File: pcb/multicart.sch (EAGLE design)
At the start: 17 parts, among them IC1 27C64-27C080, IC2 74HCT373N, IC3 74HCT08N, Q1 BS170

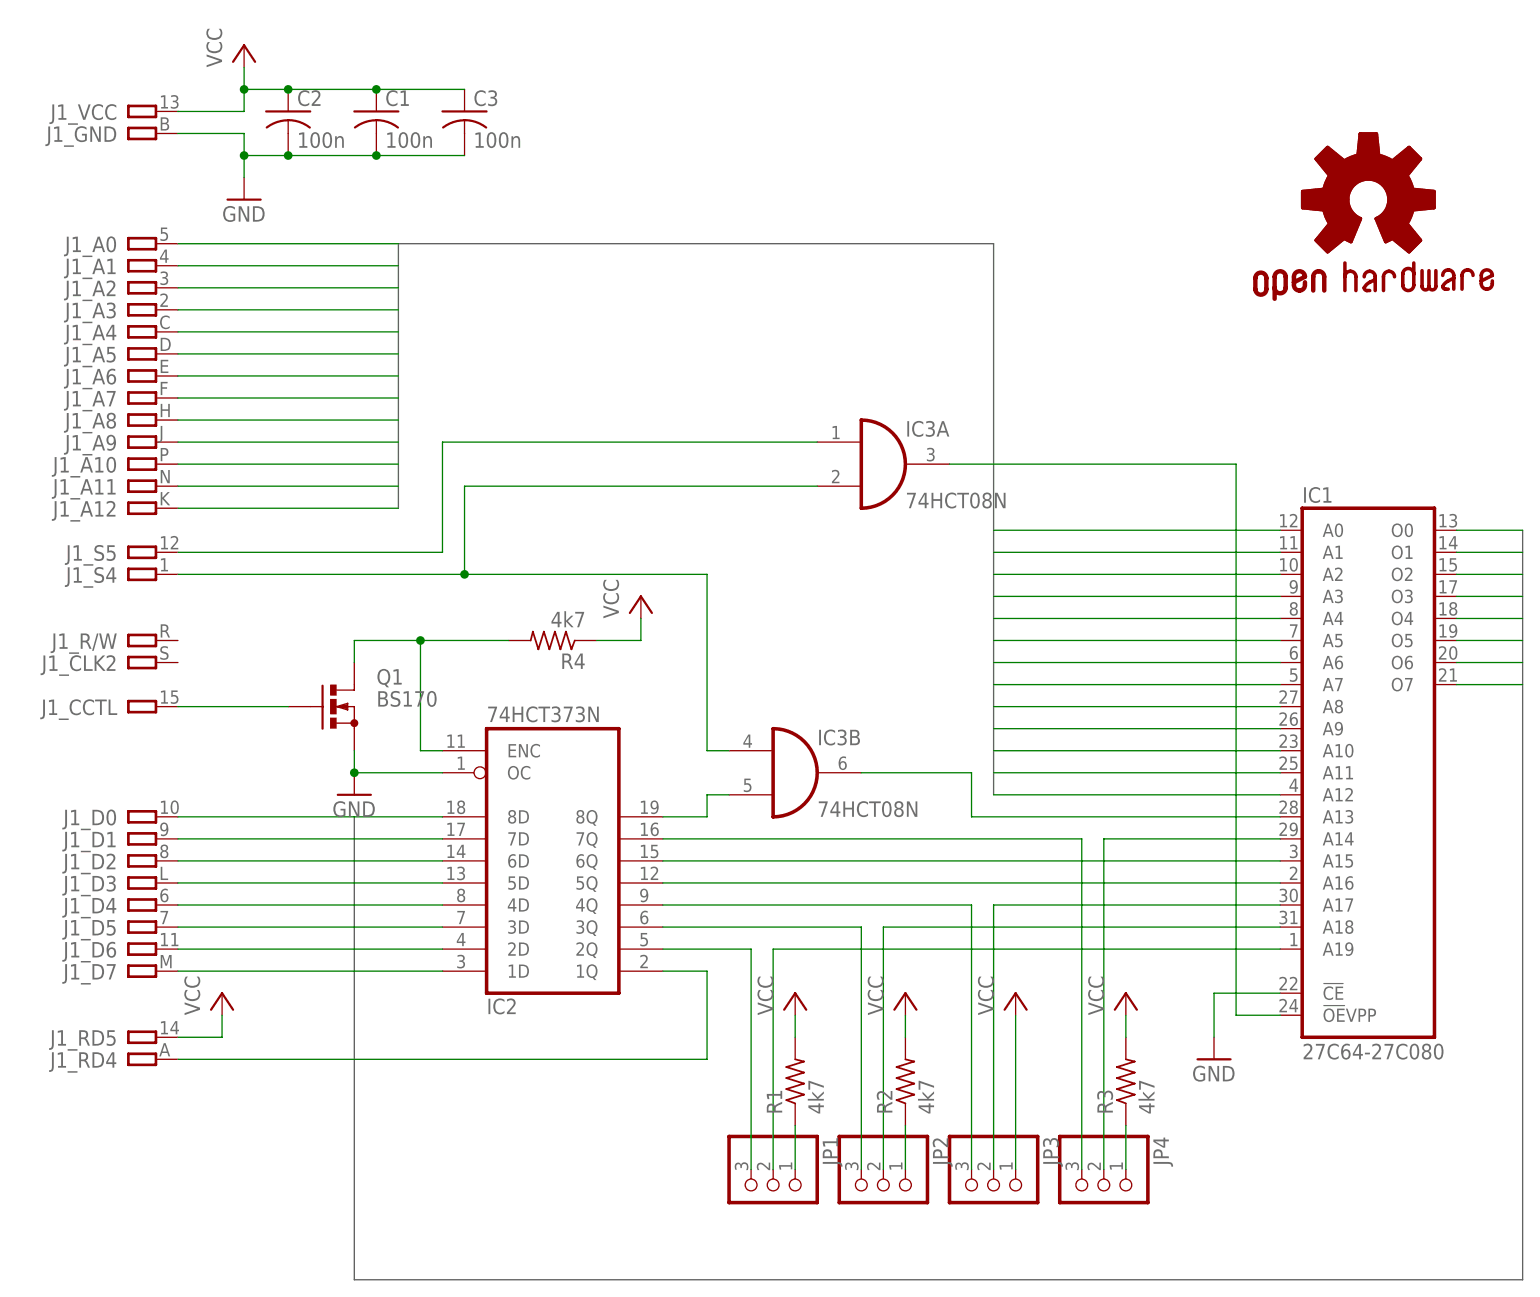
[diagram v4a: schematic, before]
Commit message: Added test points for power.
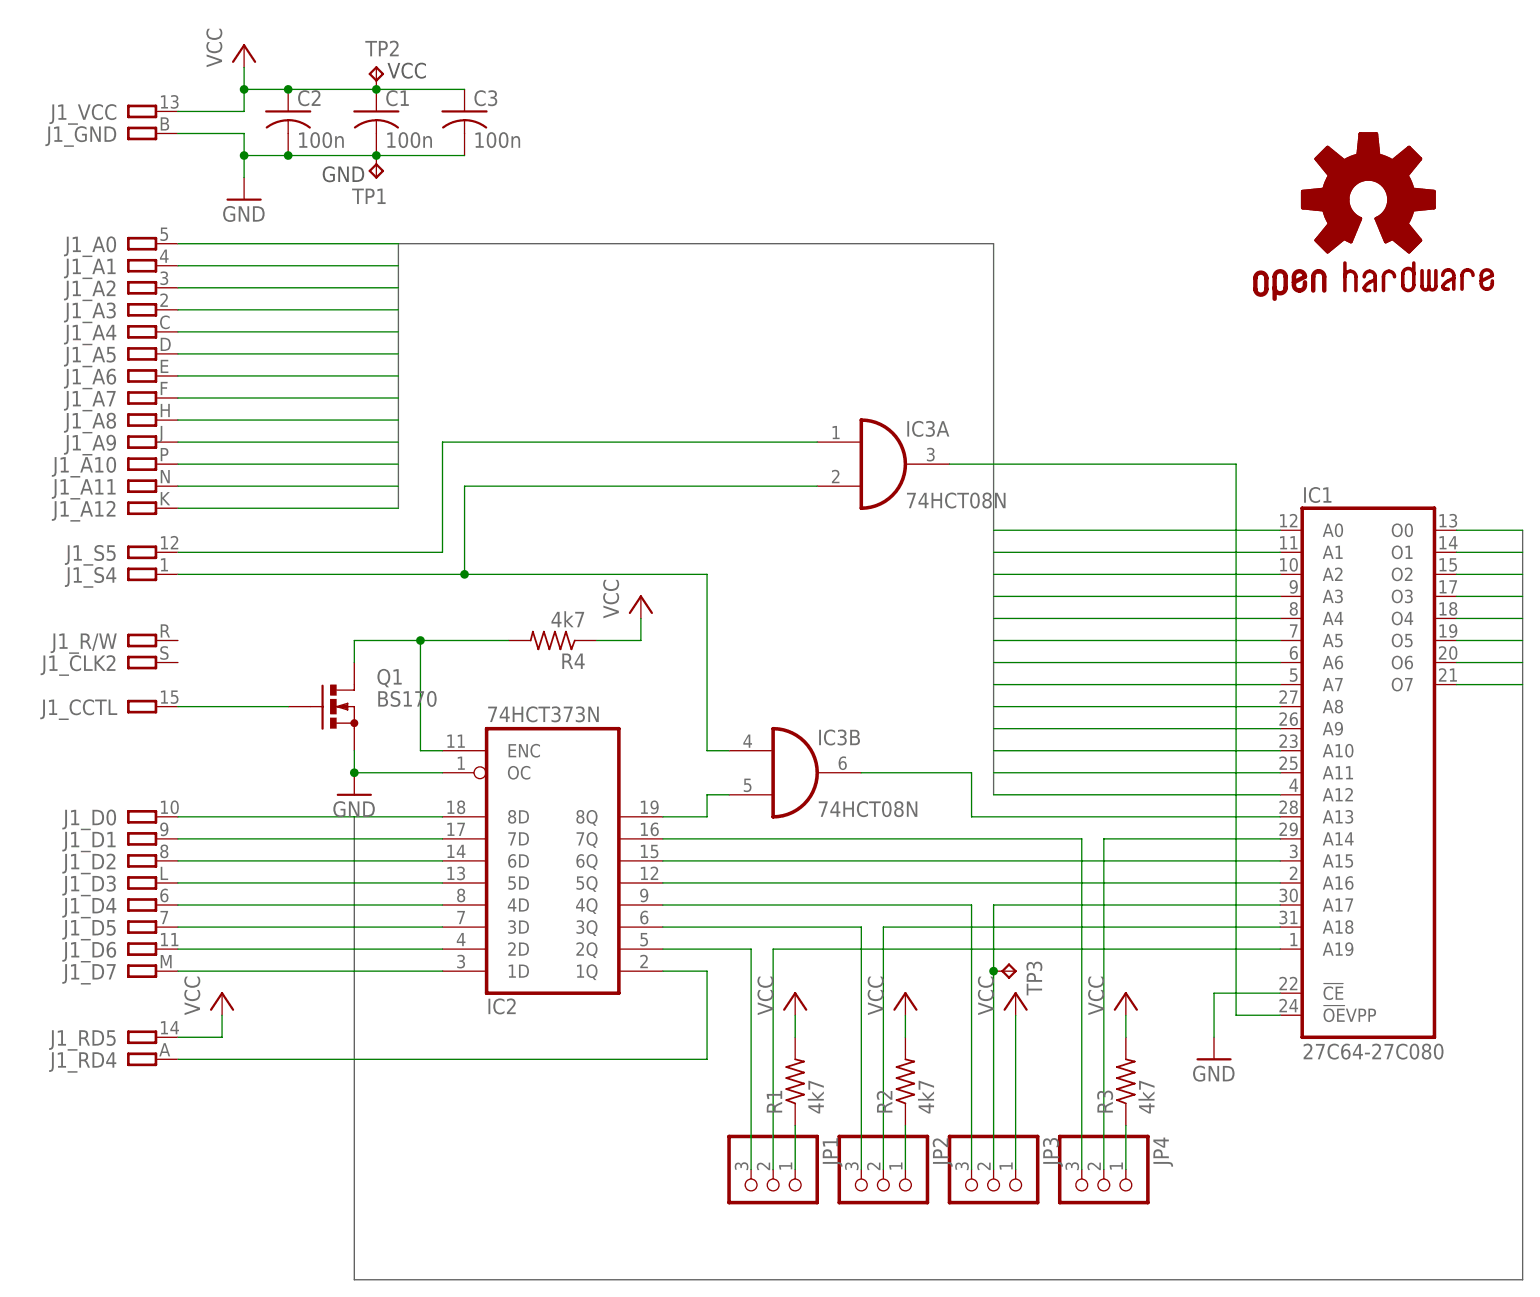
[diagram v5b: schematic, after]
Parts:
- added TP1, TP2, TP3: TPB1,27, testpad:TPB1,27
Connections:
- net GND: now also TP1.TP
- net N$12: now also TP3.TP
- net VCC: now also TP2.TP
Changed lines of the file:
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@@
 <part name="JP1" library="pinhead" deviceset="PINHD-1X3" device=""/>
 <part name="GOLD_ORB_SM1" library="bfl" deviceset="OSHWLOGO" device="_GOLD_ORB_SM"/>
+<part name="TP1" library="testpad" deviceset="TP" device="B1,27">
+<attribute name="TP_SIGNAL_NAME" value="GND"/>
+</part>
+<part name="TP2" library="testpad" deviceset="TP" device="B1,27">
+<attribute name="TP_SIGNAL_NAME" value="VCC"/>
+</part>
+<part name="TP3" library="testpad" deviceset="TP" device="B1,27">
+<attribute name="TP_SIGNAL_NAME" value="DIP28 VCC"/>
+</part>
 </parts>
 <sheets>
@@
 <instance part="JP1" gate="A" x="66.04" y="5.08" rot="R270"/>
 <instance part="GOLD_ORB_SM1" gate="G$1" x="134.62" y="119.38"/>
+<instance part="TP1" gate="G$1" x="20.32" y="121.92" rot="R180"/>
+<instance part="TP2" gate="G$1" x="20.32" y="134.62"/>
+<instance part="TP3" gate="G$1" x="93.98" y="30.48" rot="R270">
+<attribute name="TP_SIGNAL_NAME" x="93.98" y="30.48" size="1.778" layer="96" rot="R270" display="off"/>
+</instance>
 </instances>
 <busses>
@@
 <wire x1="20.32" y1="132.08" x2="30.48" y2="132.08" width="0.1524" layer="91"/>
 <junction x="20.32" y="132.08"/>
+<pinref part="TP2" gate="G$1" pin="TP"/>
 </segment>
 <segment>
@@
 <wire x1="20.32" y1="124.46" x2="30.48" y2="124.46" width="0.1524" layer="91"/>
 <junction x="20.32" y="124.46"/>
+<pinref part="TP1" gate="G$1" pin="TP"/>
 </segment>
 <segment>
@@
 <wire x1="91.44" y1="38.1" x2="124.46" y2="38.1" width="0.1524" layer="91"/>
 <pinref part="JP3" gate="A" pin="2"/>
-<wire x1="91.44" y1="38.1" x2="91.44" y2="7.62" width="0.1524" layer="91"/>
+<wire x1="91.44" y1="38.1" x2="91.44" y2="30.48" width="0.1524" layer="91"/>
 <pinref part="IC1" gate="G$1" pin="A17"/>
-</segment>
-</net>
+<pinref part="TP3" gate="G$1" pin="TP"/>
+<wire x1="91.44" y1="7.62" x2="91.44" y2="30.48" width="0.1524" layer="91"/>
+<junction x="91.44" y="30.48"/>
+</segment>
+</net>

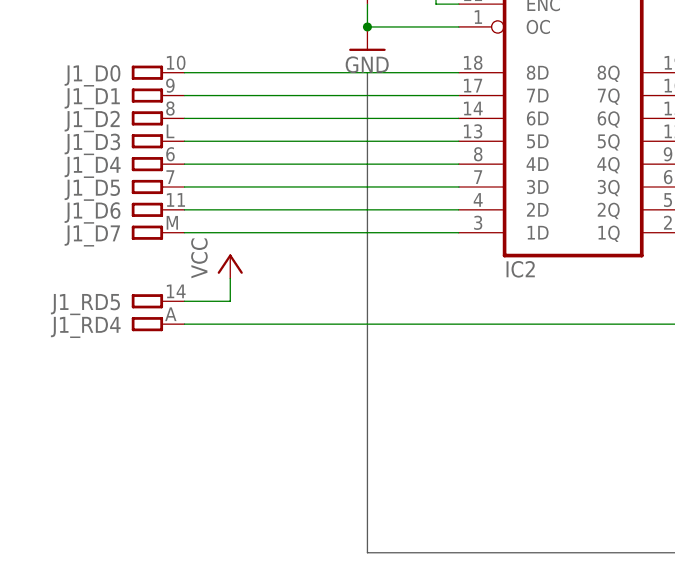
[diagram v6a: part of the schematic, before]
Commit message: Added a safety resistor to the RD5 line.
This makes it harder to break stuff when the cart is inserted upside
down.
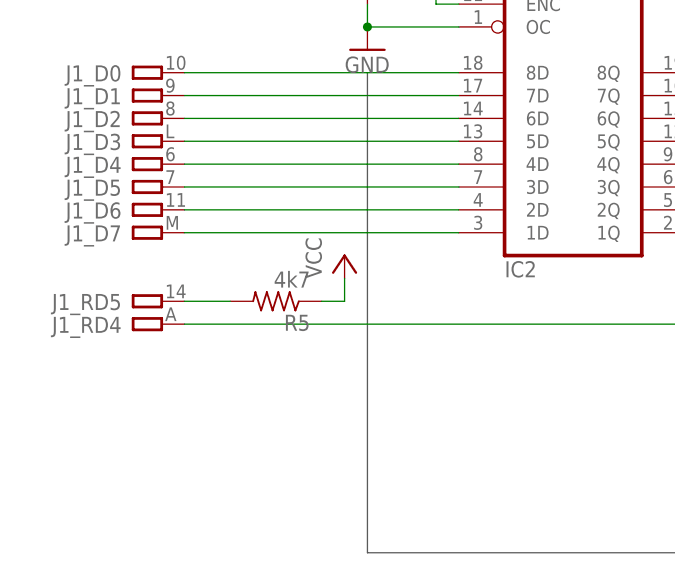
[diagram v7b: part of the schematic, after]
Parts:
- added R5: 4k7, resistor:R-US_0204/7
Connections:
- new net N$17: J1_RD5.P, R5.2
- net VCC: now also R5.1; no longer J1_RD5.P
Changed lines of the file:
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@@
 <attribute name="TP_SIGNAL_NAME" value="DIP28 VCC"/>
 </part>
+<part name="R5" library="resistor" deviceset="R-US_" device="0204/7" value="4k7"/>
 </parts>
 <sheets>
@@
 <instance part="P+1" gate="VCC" x="5.08" y="137.16"/>
 <instance part="P+2" gate="VCC" x="68.58" y="27.94"/>
-<instance part="P+4" gate="VCC" x="2.54" y="27.94"/>
+<instance part="P+4" gate="VCC" x="15.24" y="27.94"/>
 <instance part="GND4" gate="1" x="17.78" y="50.8"/>
 <instance part="GND7" gate="1" x="5.08" y="119.38"/>
@@
 <attribute name="TP_SIGNAL_NAME" x="93.98" y="30.48" size="1.778" layer="96" rot="R270" display="off"/>
 </instance>
+<instance part="R5" gate="G$1" x="7.62" y="22.86" rot="R180"/>
 </instances>
 <busses>
@@
 </net>
 <net name="VCC" class="0">
-<segment>
-<pinref part="P+4" gate="VCC" pin="VCC"/>
-<wire x1="2.54" y1="22.86" x2="2.54" y2="25.4" width="0.1524" layer="91"/>
-<pinref part="J1" gate="_RD5" pin="P"/>
-<wire x1="-2.54" y1="22.86" x2="2.54" y2="22.86" width="0.1524" layer="91"/>
-</segment>
 <segment>
 <pinref part="P+2" gate="VCC" pin="VCC"/>
@@
 <wire x1="50.8" y1="68.58" x2="50.8" y2="71.12" width="0.1524" layer="91"/>
 </segment>
+<segment>
+<pinref part="R5" gate="G$1" pin="1"/>
+<pinref part="P+4" gate="VCC" pin="VCC"/>
+<wire x1="12.7" y1="22.86" x2="15.24" y2="22.86" width="0.1524" layer="91"/>
+<wire x1="15.24" y1="22.86" x2="15.24" y2="25.4" width="0.1524" layer="91"/>
+</segment>
 </net>
 <net name="GND" class="0">
@@
 </segment>
 </net>
+<net name="N$17" class="0">
+<segment>
+<pinref part="J1" gate="_RD5" pin="P"/>
+<wire x1="-2.54" y1="22.86" x2="2.54" y2="22.86" width="0.1524" layer="91"/>
+<pinref part="R5" gate="G$1" pin="2"/>
+</segment>
+</net>
